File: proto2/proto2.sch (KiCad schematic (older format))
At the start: 10 parts, among them J12 Daughter Card, SW1 SW_DIP_x04

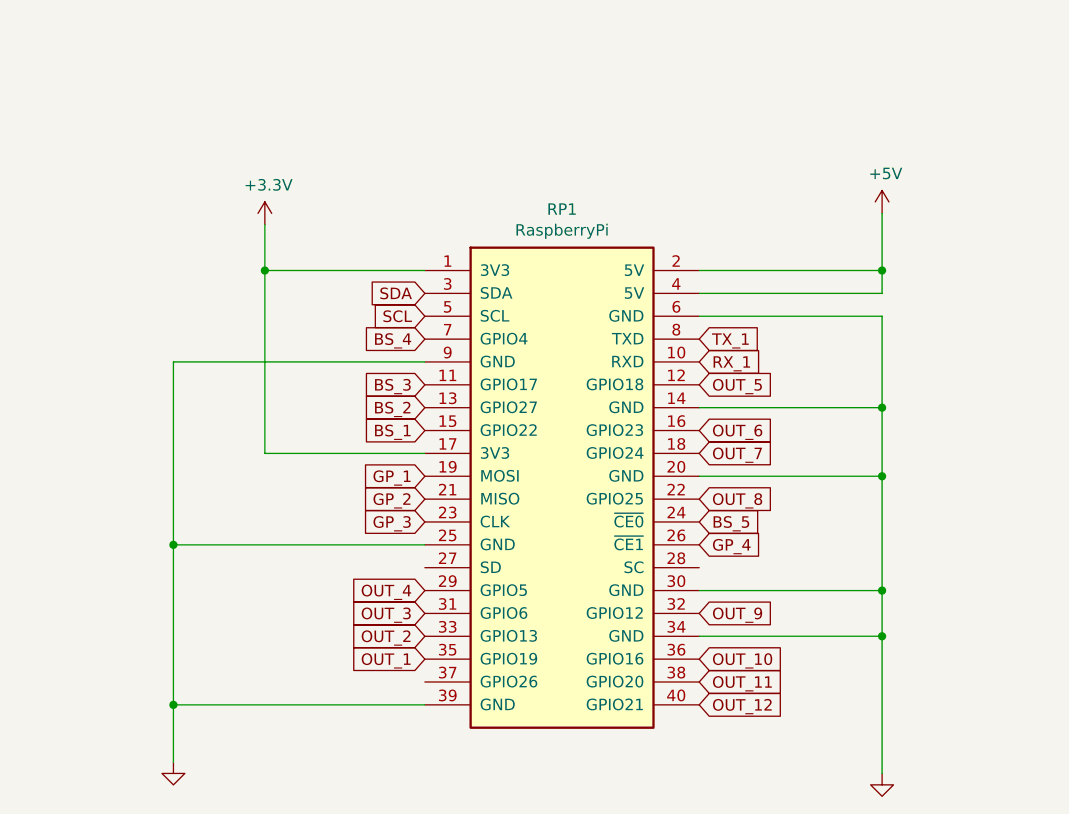
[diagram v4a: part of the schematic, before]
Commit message: Removed Raspberry Pi, added spacing to terminals.
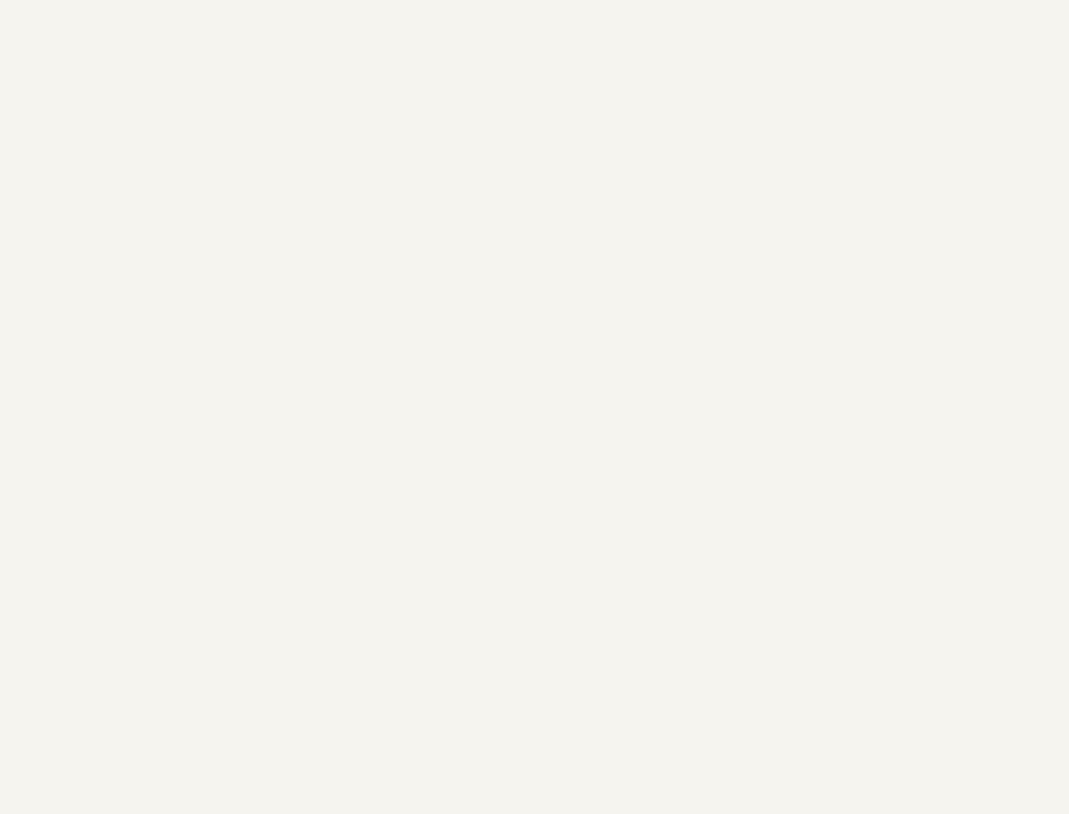
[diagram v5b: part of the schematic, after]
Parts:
- removed RP1: RaspberryPi, BCR_SBC:RaspberryPi_UpsideDown, symbol BCR:RaspberryPi
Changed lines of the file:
@@
-	1    0    0    -1
-$EndComp
-Text GLabel 2950 5450 0    50   Input ~ 0
-SCL
-Text GLabel 2950 5350 0    50   Input ~ 0
-SDA
-Wire Wire Line
-	2950 6050 2250 6050
-Wire Wire Line
-	2250 6050 2250 5250
-Connection ~ 2250 5250
-Wire Wire Line
-	2250 5250 2250 5050
-Wire Wire Line
-	2250 5250 2950 5250
-Wire Wire Line
-	4150 5350 4950 5350
-Wire Wire Line
-	4950 5350 4950 5250
-Wire Wire Line
-	4150 5250 4950 5250
-Connection ~ 4950 5250
-Wire Wire Line
-	4950 5250 4950 5000
-Wire Wire Line
-	4150 5450 4950 5450
-Wire Wire Line
-	4950 5450 4950 5850
-Wire Wire Line
-	4150 6650 4950 6650
-Connection ~ 4950 6650
-Wire Wire Line
-	4950 6650 4950 6850
-Wire Wire Line
-	4150 6150 4950 6150
-Connection ~ 4950 6150
-Wire Wire Line
-	4950 6150 4950 6650
-Wire Wire Line
-	4150 5850 4950 5850
-Connection ~ 4950 5850
-Wire Wire Line
-	4950 5850 4950 6150
-Wire Wire Line
-	2950 5650 1850 5650
-Wire Wire Line
-	1850 5650 1850 6450
-Wire Wire Line
-	2950 7150 1850 7150
-Connection ~ 1850 7150
-Wire Wire Line
-	1850 7150 1850 7400
-Wire Wire Line
-	2950 6450 1850 6450
-Connection ~ 1850 6450
-Wire Wire Line
-	1850 6450 1850 7150
-Text GLabel 4150 5650 2    50   Input ~ 0
-RX_1
-Text GLabel 4150 5550 2    50   Input ~ 0
-TX_1
-Text GLabel 2950 5950 0    50   Input ~ 0
-BS_1
-Text GLabel 2950 5850 0    50   Input ~ 0
-BS_2
-Text GLabel 2950 5750 0    50   Input ~ 0
-BS_3
-Text GLabel 2950 5550 0    50   Input ~ 0
-BS_4
-Text GLabel 2950 6950 0    50   Input ~ 0
-OUT_1
-Text GLabel 4150 5750 2    50   Input ~ 0
-OUT_5
-Text GLabel 2950 6850 0    50   Input ~ 0
-OUT_2
-Text GLabel 2950 6750 0    50   Input ~ 0
-OUT_3
-Text GLabel 2950 6650 0    50   Input ~ 0
-OUT_4
-Text GLabel 4150 5950 2    50   Input ~ 0
-OUT_6
-Text GLabel 4150 6950 2    50   Input ~ 0
-OUT_10
-Text GLabel 4150 6050 2    50   Input ~ 0
-OUT_7
-Text GLabel 4150 6250 2    50   Input ~ 0
-OUT_8
-Text GLabel 4150 6750 2    50   Input ~ 0
-OUT_9
-Text GLabel 4150 7050 2    50   Input ~ 0
-OUT_11
-Text GLabel 4150 7150 2    50   Input ~ 0
-OUT_12
-Wire Wire Line
-	4150 6850 4950 6850
-Connection ~ 4950 6850
-Wire Wire Line
-	4950 6850 4950 7450
-$Comp
-L BCR:RaspberryPi RP1
-U 1 1 61B66A11
-P 3550 6150
-F 0 "RP1" H 3550 7317 50  0000 C CNN
-F 1 "RaspberryPi" H 3550 7226 50  0000 C CNN
-F 2 "BCR_SBC:RaspberryPi_UpsideDown" V 3050 4350 50  0001 L CNN
-F 3 "" V 2800 6600 50  0001 C CNN
-	1    3550 6150
 	1    0    0    -1
 $EndComp
@@
 F 3 "" H 4600 1000 50  0001 C CNN
 	1    4600 1000
-	1    0    0    -1
-$EndComp
-$Comp
-L power:+3.3V #PWR014
-U 1 1 61BF2645
-P 2250 5050
-F 0 "#PWR014" H 2250 4900 50  0001 C CNN
-F 1 "+3.3V" H 2265 5223 50  0000 C CNN
-F 2 "" H 2250 5050 50  0001 C CNN
-F 3 "" H 2250 5050 50  0001 C CNN
-	1    2250 5050
 	1    0    0    -1
 $EndComp
@@
 $EndComp
 $Comp
-L power:GND #PWR017
-U 1 1 61BA3383
-P 4950 7450
-F 0 "#PWR017" H 4950 7200 50  0001 C CNN
-F 1 "GND" H 4955 7277 50  0001 C CNN
-F 2 "" H 4950 7450 50  0001 C CNN
-F 3 "" H 4950 7450 50  0001 C CNN
-	1    4950 7450
-	1    0    0    -1
-$EndComp
-$Comp
-L power:GND #PWR016
-U 1 1 61BA3D13
-P 1850 7400
-F 0 "#PWR016" H 1850 7150 50  0001 C CNN
-F 1 "GND" H 1855 7227 50  0001 C CNN
-F 2 "" H 1850 7400 50  0001 C CNN
-F 3 "" H 1850 7400 50  0001 C CNN
-	1    1850 7400
-	1    0    0    -1
-$EndComp
-$Comp
 L power:GND #PWR015
 U 1 1 61BA4111
@@
 F 3 "~" H 9050 1750 50  0001 C CNN
 	1    9050 1750
-	1    0    0    -1
-$EndComp
-$Comp
-L power:+5V #PWR013
-U 1 1 61BF2EBE
-P 4950 5000
-F 0 "#PWR013" H 4950 4850 50  0001 C CNN
-F 1 "+5V" H 4965 5173 50  0000 C CNN
-F 2 "" H 4950 5000 50  0001 C CNN
-F 3 "" H 4950 5000 50  0001 C CNN
-	1    4950 5000
 	1    0    0    -1
 $EndComp
@@
 Text GLabel 1550 1900 0    50   Input ~ 0
 OUT_1
-Text GLabel 4150 6350 2    50   Input ~ 0
-BS_5
 Text GLabel 2950 3500 2    50   Input ~ 0
 BS_5
@@
 Text GLabel 2950 3000 2    50   Input ~ 0
 GP_4
-Text GLabel 2950 6250 0    50   Input ~ 0
-GP_2
-Text GLabel 2950 6150 0    50   Input ~ 0
-GP_1
-Text GLabel 2950 6350 0    50   Input ~ 0
-GP_3
-Text GLabel 4150 6450 2    50   Input ~ 0
-GP_4
 Text GLabel 9250 4050 0    50   Input ~ 0
